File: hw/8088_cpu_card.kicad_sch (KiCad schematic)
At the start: 22 parts, among them J1 80188, J2 PC XT ISA, SW1 RESET, U1 GAL16V8, U2 SN74ABT16841DL, U3 74LS245, U5 SRAM, Y1 16MHz

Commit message: kinda working revision
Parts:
- added J5: 8259, Package_LCC:PLCC-28_THT-Socket, symbol Interface:8259
- added JP1, JP2: (no value), Jumper:SolderJumper-3_P1.3mm_Open_RoundedPad1.0x1.5mm, symbol Jumper:SolderJumper_3_Open
- added R4: Limit, Resistor_SMD:R_1206_3216Metric_Pad1.30x1.75mm_HandSolder, symbol Device:R_Small
- J1: footprint 8468-11B1-RK-TP:846811B1RKTP -> 80C188:PGA68-N
- J4: renamed from U4; value (none) -> SST39SF020; footprint (none) -> Package_LCC:PLCC-32_THT-Socket
- R2, R3: value PullUP -> Limit
- renumbered U1 to J3, U2 to U1, U3 to U2, U5 to U3
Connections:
- net +5VD: now also R3.1, J5.28 (VCC), R4.1; no longer R3.2
- net A0: now also J5.27 (A0)
- net DB0: now also J5.11 (D0)
- net DB1: now also J5.10 (D1)
- net DB2: now also J5.9 (D2)
- net DB3: now also J5.8 (D3)
- net DB4: now also J5.7 (D4)
- net DB5: now also J5.6 (D5)
- net DB6: now also J5.5 (D6)
- net DB7: now also J5.4 (D7)
- net DRQ0: now also J2.18 (DRQ1)
- net DRQ1: now also J2.6 (DRQ2); no longer J2.18 (DRQ1)
- net GNDD: now also U2.10 (GND), J5.14 (GND)
- net INT0: now also J5.17 (INT)
- net ~{CARDSLCTD}: now also J3.8 (I8); no longer J3.7 (I7), R2.2
- net ~{DEN}: now also J3.9 (I9); no longer J3.8 (I8)
- net ~{IOR}: now also J5.3 (~{RD})
- net ~{IOW}: now also J5.2 (~{WR})
- net ~{PCS4}: now also J2.17 (~{DACK1})
- net ~{PCS5}: now also J2.26 (~{DACK2})
- net ~{PCS6}: now also J2.15 (~{DACK3})
- net ~{UCS}: no longer J3.6 (I6)
- net ~{PCS3}: now reaches J2.19 (~{DACK0})
- net ~{PCS3}: now also J1.29 (~{PCS3})
- net IR7: now reaches J2.21 (IRQ7)
- net IR7: now also J5.25 (IR7)
- net IR6: now reaches J2.22 (IRQ6)
- net IR6: now also J5.24 (IR6)
- net IR5: now reaches J2.23 (IRQ5)
- net IR5: now also J5.23 (IR5)
- net IR4: now reaches J2.24 (IRQ4)
- net IR4: now also J5.22 (IR4)
- net IRQ3: now reaches J2.25 (IRQ3)
- net IRQ3: now also JP2.2 (C)
- net IRQ2: now reaches J2.4 (IRQ2)
- net IRQ2: now also JP1.2 (C)
- net at J1.20 (TMR_IN_0): now also R4.2
- net ~{CS_I}: now reaches J1.27 (~{PCS1})
- net ~{CS_I}: now also J3.6 (I6), J5.1 (~{CS})
- net INT3: now reaches J1.41 (INT3/~{INTA1}/IRQ)
- net INT3: now also JP2.3 (B)
- net INT1: now reaches J1.44 (INT1/~{SELECT})
- net INT1: now also JP1.3 (B)
- net at J1.49 (SRDY): now also R3.2
- net at J1.55 (ARDY): now also R2.2
- net INT2 renamed ~{INTA0}
- net ~{INTA0}: now also J5.26 (~{INTA})
- net TMR_OUT_0 renamed BAUD
- net ~{PCS0} renamed ~{CS_S}
- net ~{CS_S}: now also J3.7 (I7)
- removed net ~{PGMENA}: J3.9 (I9), R3.1
- net ~{PGM}: no longer names the net of J4.31 (~{PGM})
- net ~{PGM}: no longer J3.12 (IO8)
- new net IR0: J5.18 (IR0)
- new net IR1: J5.19 (IR1)
- new net IR2: J5.20 (IR2), JP1.1 (A)
- new net IR3: J5.21 (IR3), JP2.1 (A)
- no-connect marks 40 -> 31
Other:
- moved on the sheet: C1, C10, C2, C3, C4, C5, C6, C7, C8, C9, J1, J2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

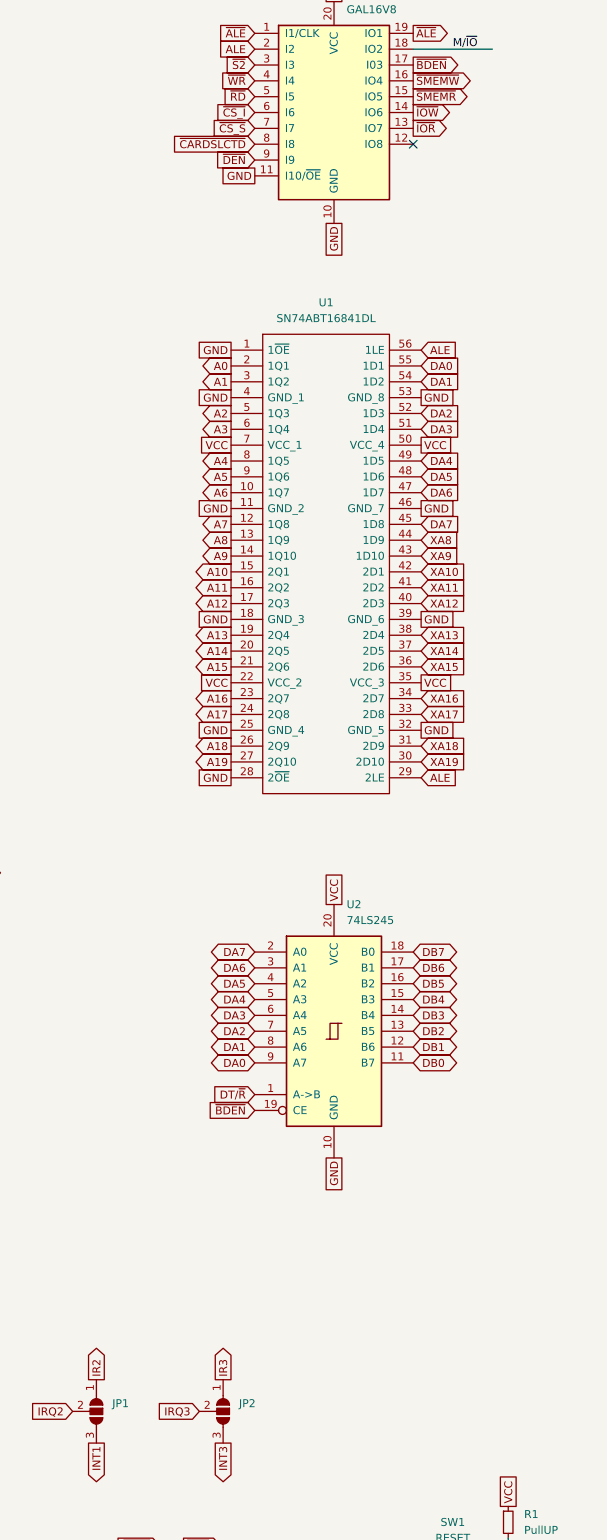
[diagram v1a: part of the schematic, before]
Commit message: minimal viable board
* PLD provides /IOW and TRG signals for reading all IO out
* BIOS initialises the /UMCS and print debug
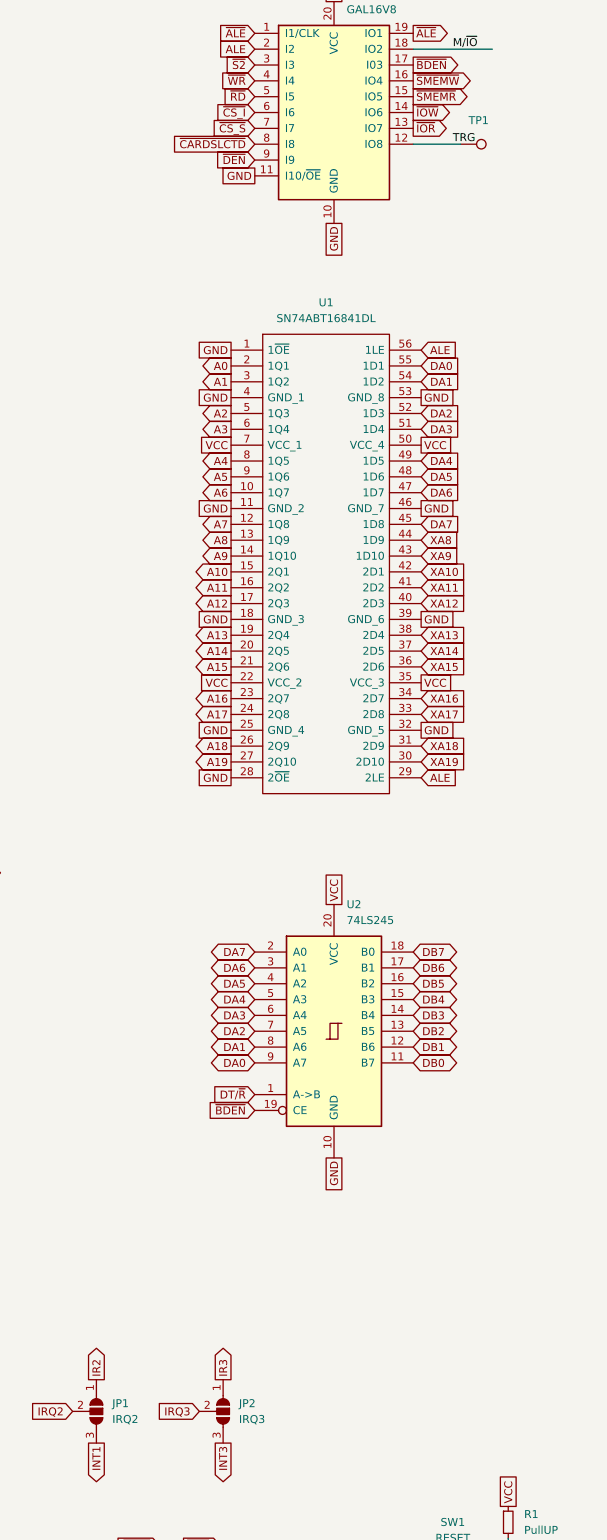
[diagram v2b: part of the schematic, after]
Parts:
- added TP1: (no value), symbol Connector:TestPoint
- JP1: value (none) -> IRQ2
- JP2: value (none) -> IRQ3
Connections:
- net TRG: now reaches J3.12 (IO8)
- net TRG: now also TP1.1
- no-connect marks 31 -> 30
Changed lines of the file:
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@@
   (no_connect (at 109.22 40.64))
   (no_connect (at 114.3 40.64))
-  (no_connect (at 232.41 43.18))
   (no_connect (at 153.67 96.52))
   (wire (pts (xy 128.27 265.43) (xy 148.59 265.43))
@@
     (stroke (width 0) (type default) (color 0 0 0 0))
   )
+  (wire (pts (xy 240.03 43.18) (xy 232.41 43.18))
+    (stroke (width 0) (type default) (color 0 0 0 0))
+  )
   (wire (pts (xy 90.17 265.43) (xy 109.22 265.43))
     (stroke (width 0) (type default) (color 0 0 0 0))
@@
     (effects (font (size 1.27 1.27)) (justify left bottom))
   )
+  (label "TRG" (at 238.76 43.18 0)
+    (effects (font (size 1.27 1.27)) (justify left bottom))
+  )
   (label "M{slash}~{IO}" (at 238.76 27.94 0)
     (effects (font (size 1.27 1.27)) (justify left bottom))
@@
     (pin "1")
     (pin "2")
+  )
+  (symbol (lib_id "Connector:TestPoint") (at 240.03 43.18 270) (unit 1)
+    (in_bom yes) (on_board yes)
+    (property "Reference" "TP1" (id 0) (at 241.3 39.37 90)
+      (effects (font (size 1.27 1.27)) (justify left))
+    )
+    (property "Value" "" (id 1) (at 241.3 45.72 90)
+      (effects (font (size 1.27 1.27)) (justify left))
+    )
+    (property "Footprint" "" (id 2) (at 240.03 48.26 0)
+      (effects (font (size 1.27 1.27)) hide)
+    )
+    (property "Datasheet" "~" (id 3) (at 240.03 48.26 0)
+      (effects (font (size 1.27 1.27)) hide)
+    )
+    (pin "1")
   )
   (symbol (lib_id "Device:C_Small") (at 247.65 273.05 0) (unit 1)
@@
       (effects (font (size 1.27 1.27)) (justify left))
     )
-    (property "Value" "" (id 1) (at 184.15 247.6499 90)
+    (property "Value" "IRQ2" (id 1) (at 184.15 247.6499 90)
       (effects (font (size 1.27 1.27)) (justify left))
     )
@@
       (effects (font (size 1.27 1.27)) (justify left))
     )
-    (property "Value" "" (id 1) (at 204.47 247.6499 90)
+    (property "Value" "IRQ3" (id 1) (at 204.47 247.6499 90)
       (effects (font (size 1.27 1.27)) (justify left))
     )
@@
       (reference "SW1") (unit 1) (value "RESET") (footprint "Button_Switch_SMD:SW_SPST_EVQP7A")
     )
+    (path "/1d968e22-8dd8-4fac-a007-c642fea56cbe"
+      (reference "TP1") (unit 1) (value "TRG") (footprint "TestPoint:TestPoint_Pad_1.0x1.0mm")
+    )
     (path "/587bfaf1-ba31-4f37-8d48-72095776464f"

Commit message: board fixes
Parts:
- removed C3: 1u BTN, Capacitor_SMD:C_0805_2012Metric_Pad1.18x1.45mm_HandSolder, symbol Device:C_Small
- removed R1: PullUP, Resistor_SMD:R_1206_3216Metric_Pad1.30x1.75mm_HandSolder, symbol Device:R_Small
- removed TP1: (no value), symbol Connector:TestPoint
- added U4: (no value), symbol Power_Supervisor:TCM809
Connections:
- net TRG is gone; now on net RESET: J3.12 (IO8)
- net +5VD: now also U4.3 (VCC)
- net GNDD: now also U4.1 (GND)
- net RESET: no longer J1.57 (RESET)
- net ~{CS_I}: no longer J3.6 (I6)
- net ~{RES}: now also J3.6 (I6), U4.2 (~{RESET})
- no-connect marks 30 -> 33
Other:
- note added: "ToDo 1. Current limiting R 2. INT2 as INTA 3. DT/R generates on GAL for debug purposes 4. HLDA for driving the local bus"
- note removed: "ToDo 1. Current limiting R 2. INT2 as INTA Wishlist 1. 2nd timer and 8255 IO for speaker 2. IRQ and 8255 for KBD"
- moved on the sheet: J3, U1, U2
